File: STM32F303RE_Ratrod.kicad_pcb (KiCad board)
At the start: 2 copper layers, 45.1 x 50.8 mm, 37 parts, among them J1 USB_B_Micro, J2 CONN_01X02, J3 Barrel_Jack_Switch, J4 PROG, J5 Power Pass-thru, J6 CONN_02X12, J7 CONN_02X12, J8 CONN_02X02, U1 AZ1117-3.3, U2 STM32F303RETx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

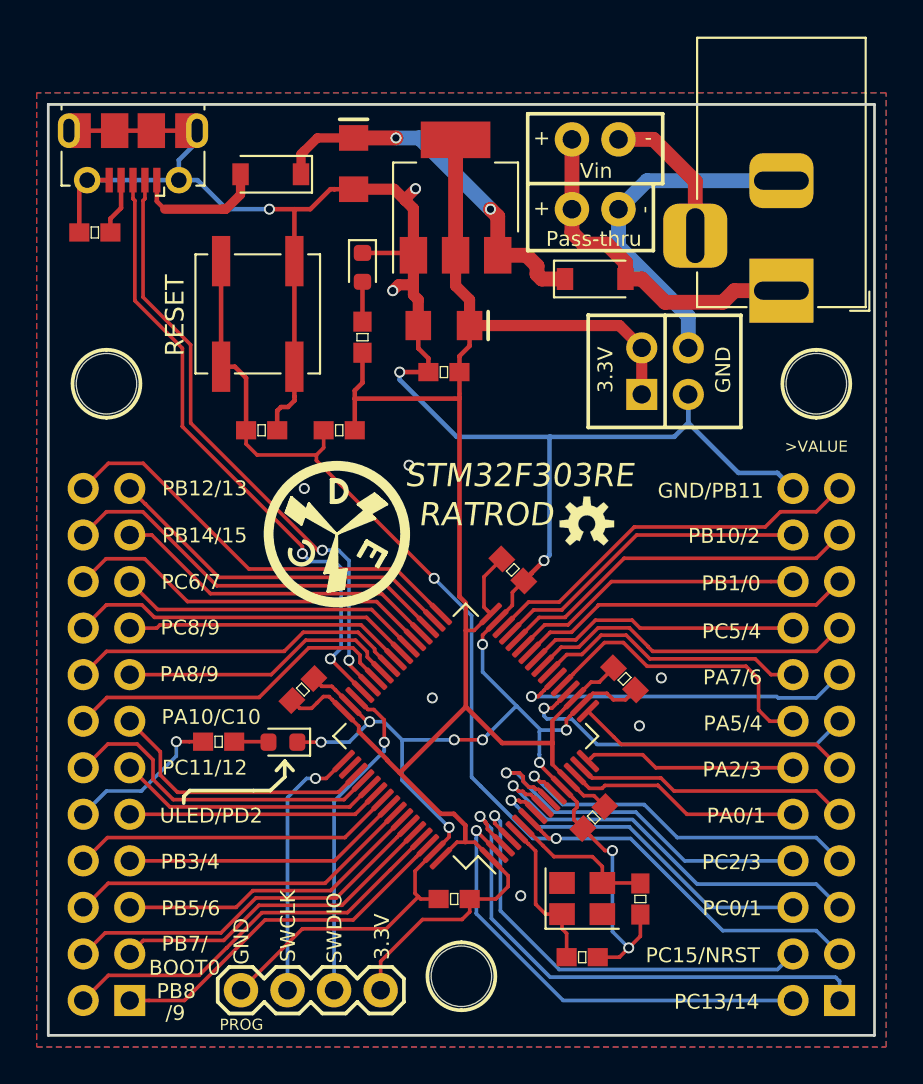
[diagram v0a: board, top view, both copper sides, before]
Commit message: Moved a couple caps, put labels on the bottom, fixed logos.
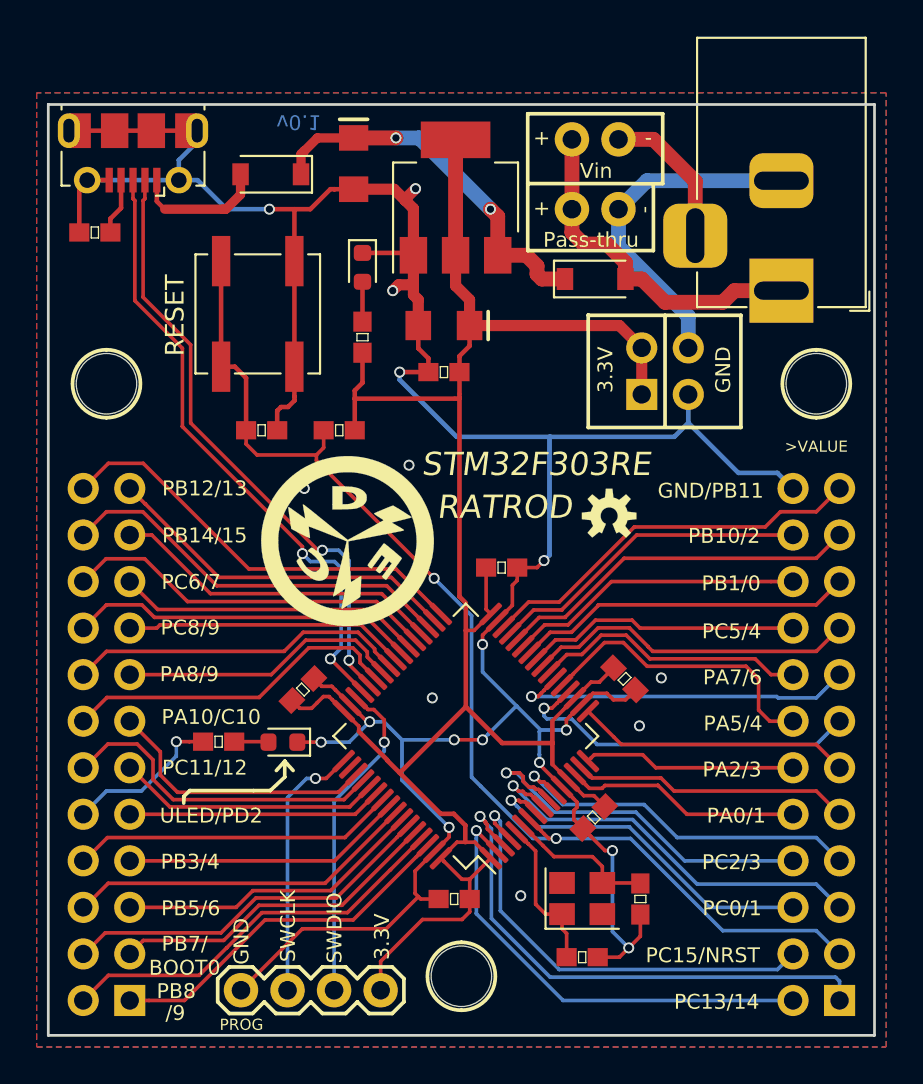
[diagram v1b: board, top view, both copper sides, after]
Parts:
- removed the ? at (149.5, 105.5)
- removed DEC_small: DEC_small, Pete:DEC_small
- added ?: , Aesthetics:OSHW-LOGO-S, B.Cu at (150.4, 83.9)
- added G***: LOGO, Pete:DEC_23mm, B.Cu at (149.9, 108.1)
- added G***: LOGO, Pete:DEC_10mm, F.Cu at (143.3, 99.5)
- added G***: LOGO, Pete:Checkered_Flag, B.Cu at (136.9, 84.2)
- moved ? 1.29 mm to (157.6, 98.7)
- moved C8 0.62 mm to (151.7, 101.5), turned to 0 degrees
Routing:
- net GND: track 191.1 -> 191.7 mm
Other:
- board text added: "v0.1"
